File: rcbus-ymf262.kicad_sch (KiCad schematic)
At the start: 36 parts, among them CON1 SJ1-3523N, P1 RC2014 BUS, U1 74HCT688, U2 YMF262, U5 YAC512, U6 TL074, X1 14.318MHz

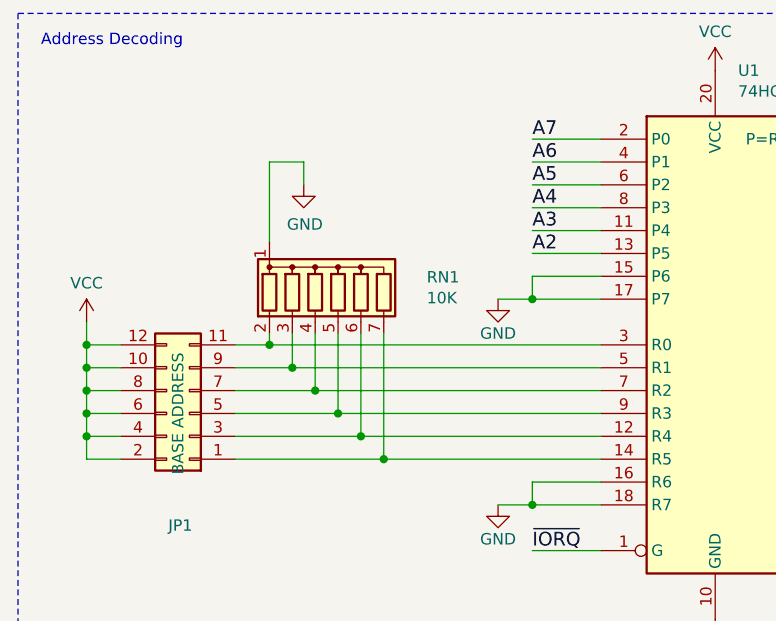
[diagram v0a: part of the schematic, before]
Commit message: some more routing, use individual resistors, change name to rcbus
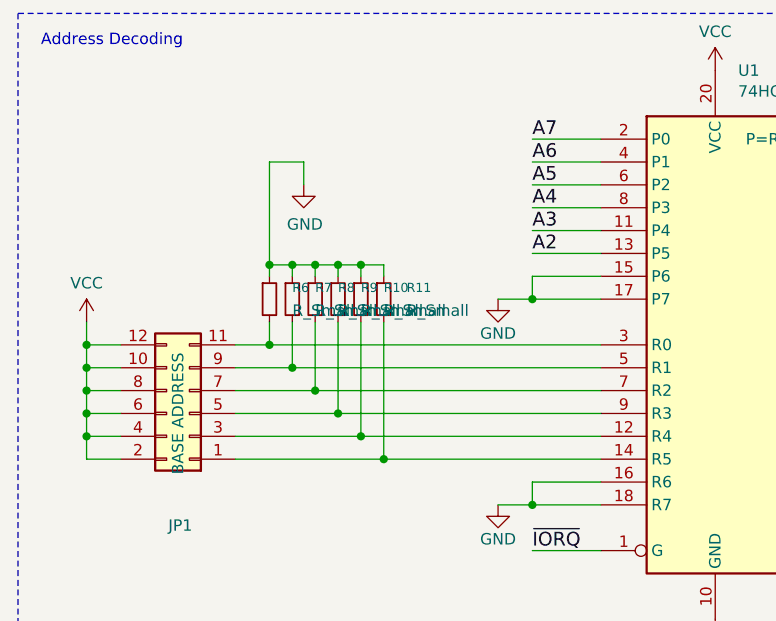
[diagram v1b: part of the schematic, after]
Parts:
- removed RN1: 10K, Resistor_SMD:R_Array_Convex_8x0602, symbol Device:R_Network06
- added R10, R11, R6, R7, R8, R9: R_Small, Resistor_SMD:R_0603_1608Metric_Pad0.98x0.95mm_HandSolder, symbol Device:R_Small
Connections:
- net GND: now also R10.1, R11.1, R6.1, R7.1, R8.1, R9.1
- net at JP1.1 (Pin_1), U1.14 (R5): now also R11.2
- net at JP1.11 (Pin_11), U1.3 (R0): now also R6.2
- net at JP1.3 (Pin_3), U1.12 (R4): now also R10.2
- net at JP1.5 (Pin_5), U1.9 (R3): now also R9.2
- net at JP1.7 (Pin_7), U1.7 (R2): now also R8.2
- net at JP1.9 (Pin_9), U1.5 (R1): now also R7.2
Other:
- title: RC2014 YM3812 sound card -> RCBUS YMF262 sound card

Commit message: more routing
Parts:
- R10, R11, R6, R7, R8, R9: value R_Small -> 10K
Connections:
- net +5V is gone; now on net VCC: C1.1, L1.2
- net GND: now also R10.2, R11.2, R6.2, R7.2, R8.2, R9.2; no longer R10.1, R11.1, R6.1, R7.1, R8.1, R9.1
- net at JP1.1 (Pin_1), U1.14 (R5): now also R11.1; no longer R11.2
- net at JP1.11 (Pin_11), U1.3 (R0): now also R6.1; no longer R6.2
- net at JP1.3 (Pin_3), U1.12 (R4): now also R10.1; no longer R10.2
- net at JP1.5 (Pin_5), U1.9 (R3): now also R9.1; no longer R9.2
- net at JP1.7 (Pin_7), U1.7 (R2): now also R8.1; no longer R8.2
- net at JP1.9 (Pin_9), U1.5 (R1): now also R7.1; no longer R7.2
- net AUDIO_CH2: now reaches C10.1, U5.11 (CH2), U6.10 (+)
- net AUDIO_CH1: now reaches C11.1, U5.10 (CH1), U6.12 (+)
- no-connect marks 21 -> 22
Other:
- moved on the sheet: C17, R10, R11, R6, R7, R8, R9

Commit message: pcb updates, remove old github actions
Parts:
- removed C15: 100nf, Capacitor_SMD:C_0603_1608Metric_Pad1.08x0.95mm_HandSolder, symbol Device:C_Small
- renumbered C2 to C1, C11 to C10, C5 to C11, C7 to C12, C16 to C13, C17 to C14, C12 to C15, C14 to C16, C18 to C17, C19 to C18, C1 to C2, C8 to C3, C9 to C4, C13 to C5, C3 to C6, C4 to C7, C6 to C8, C10 to C9, R6 to R1, R4 to R10, R5 to R11, R7 to R2, R8 to R3, R9 to R4, R10 to R5, R11 to R6, R1 to R7, R2 to R8, R3 to R9, U5 to U3, U6 to U4

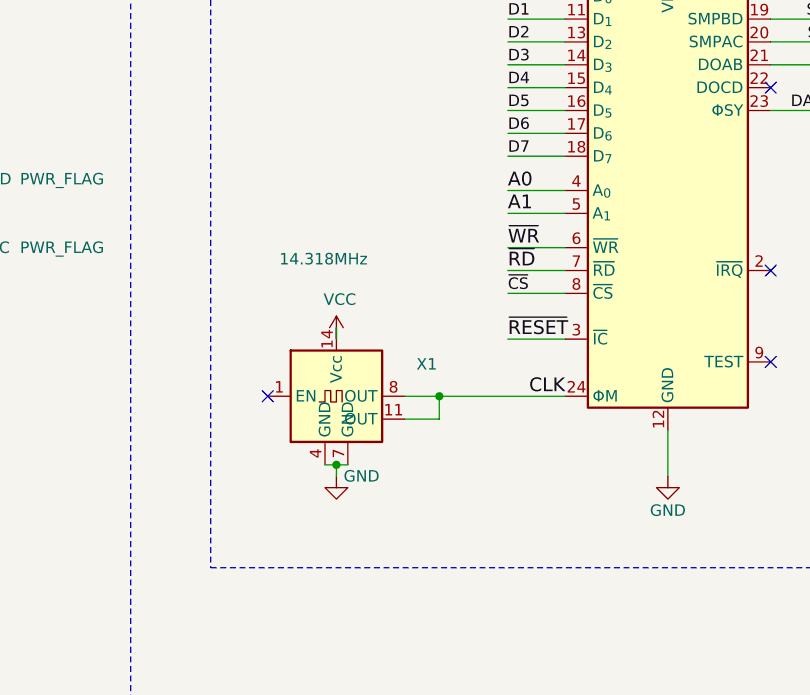
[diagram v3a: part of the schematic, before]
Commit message: use smd oscillator
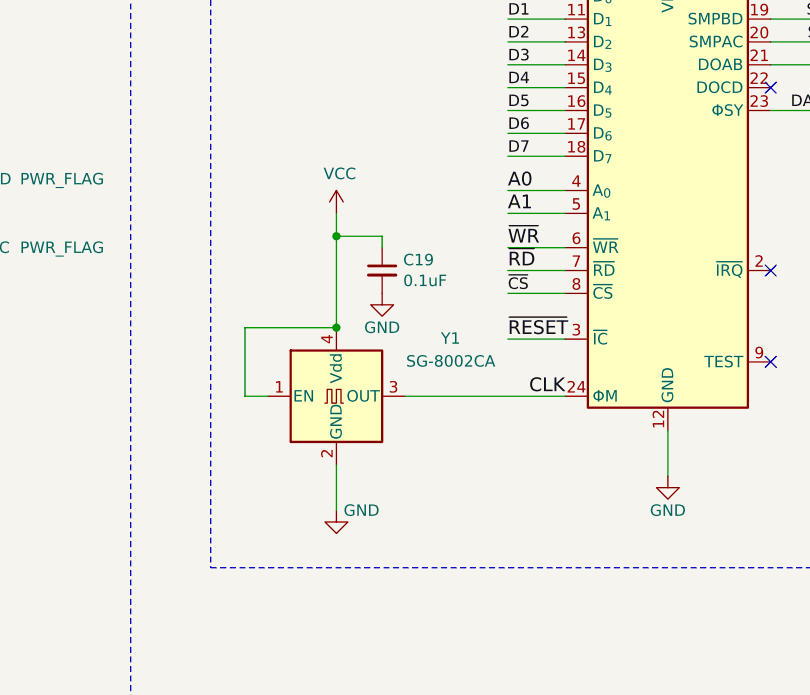
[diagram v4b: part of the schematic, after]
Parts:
- removed X1: 14.318MHz, electrified:Oscillator_DIP-8-14, symbol electrified:CXO_DIP-8-14
- added C19: 0.1uF, Capacitor_SMD:C_0603_1608Metric_Pad1.08x0.95mm_HandSolder, symbol Device:C_Small
- added Y1: SG-8002CA, Oscillator:Oscillator_SMD_Abracon_ASV-4Pin_7.0x5.1mm, symbol Oscillator:ASV-xxxMHz
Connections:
- net CLK: now also Y1.3 (OUT)
- net GND: now also C19.2, Y1.2 (GND)
- net VCC: now also C19.1, Y1.1 (EN), Y1.4 (Vdd)
- no-connect marks 22 -> 21

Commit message: set version no
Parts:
- C8: symbol Device:C_Small -> Device:C_Polarized_Small
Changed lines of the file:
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@@
 	)
 	(symbol
-		(lib_id "Device:C_Small")
+		(lib_id "Device:C_Polarized_Small")
 		(at 262.89 80.01 0)
 		(unit 1)
@@
 			)
 		)
-		(property "Description" "Unpolarized capacitor, small symbol"
+		(property "Description" "Polarized capacitor, small symbol"
 			(at 262.89 80.01 0)
 			(effects

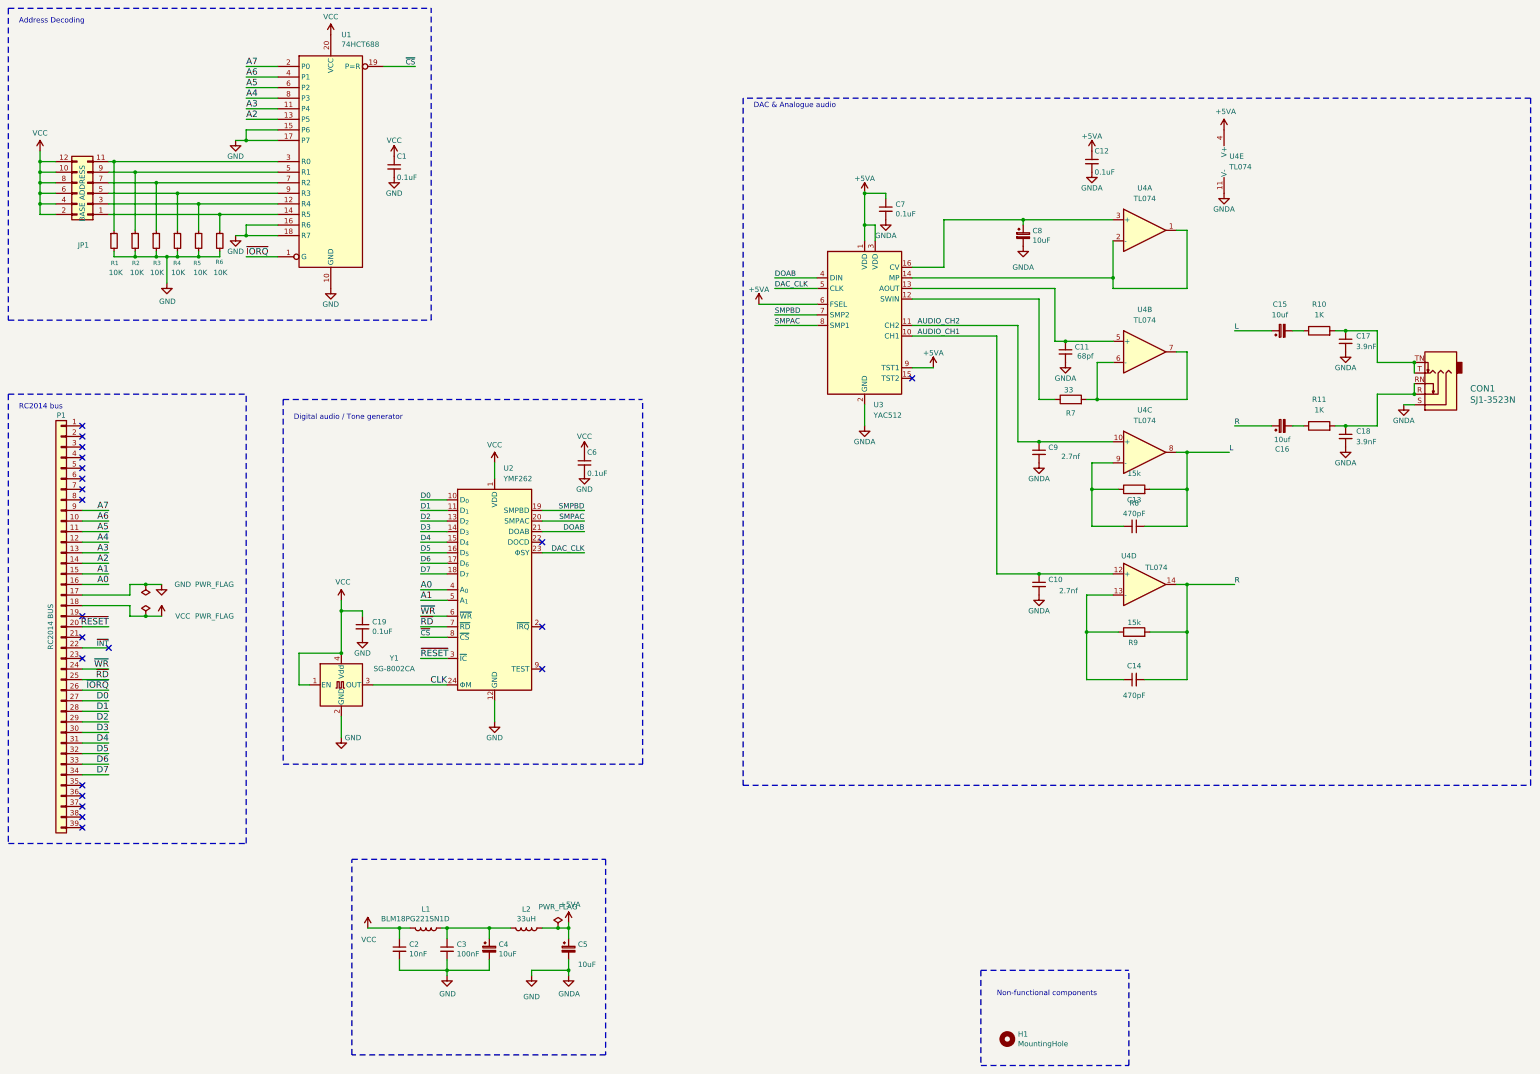
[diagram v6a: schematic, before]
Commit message: remove gnda, another attempt at versioning
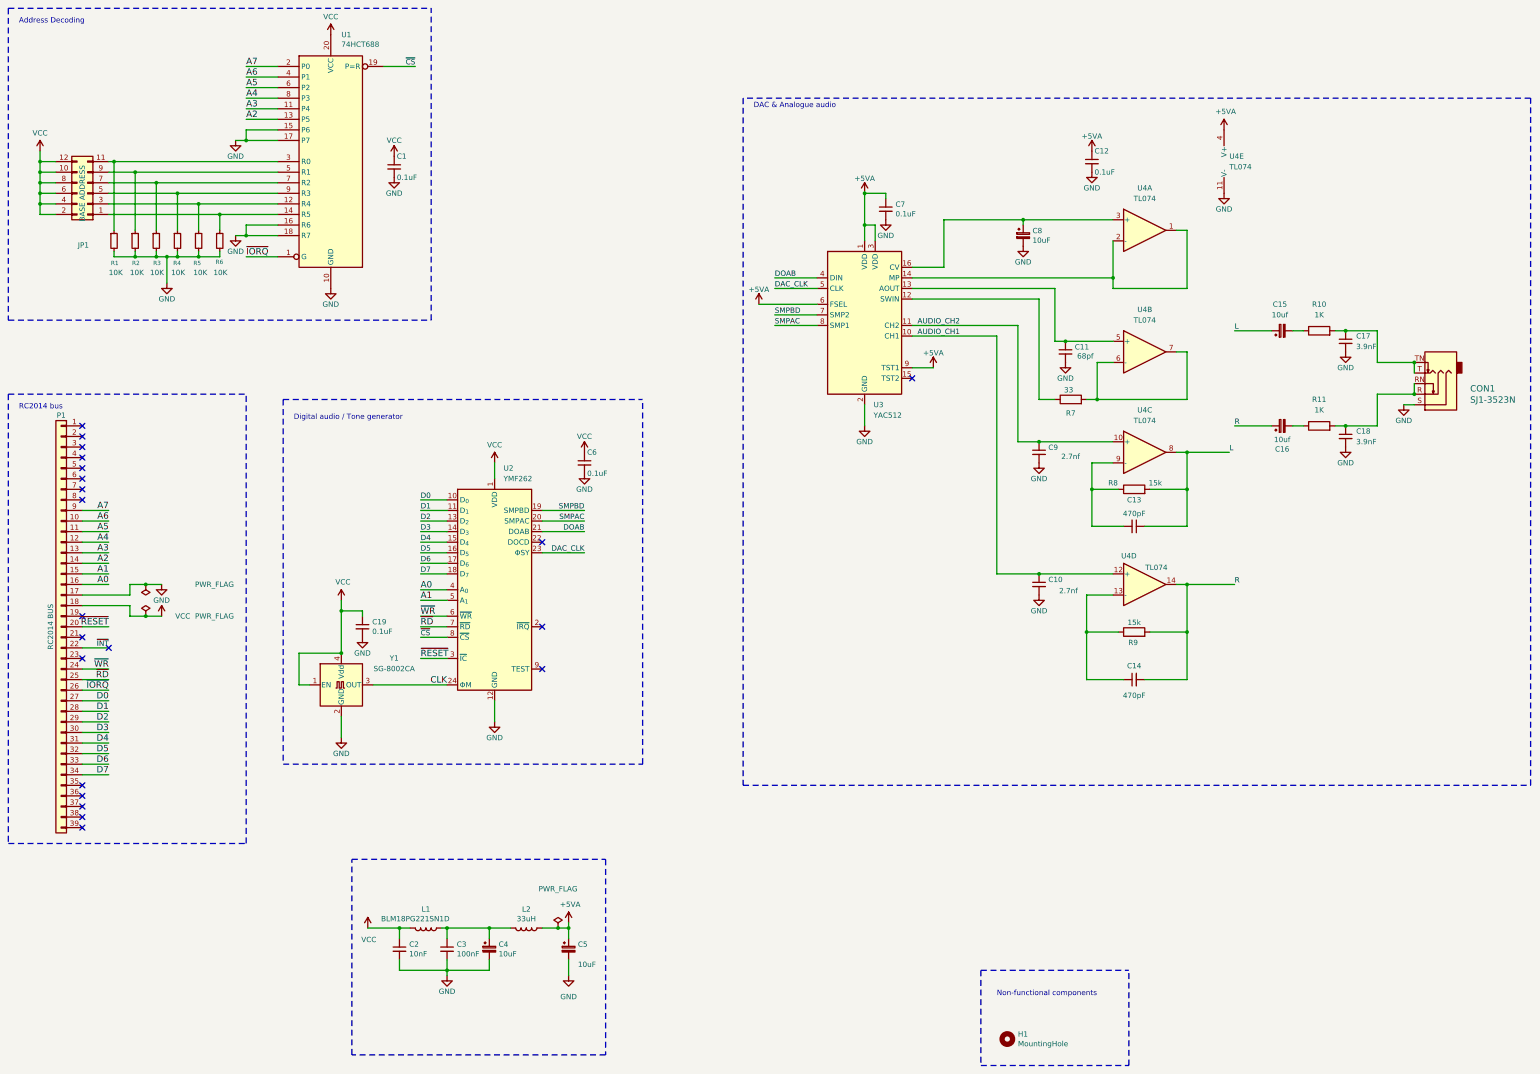
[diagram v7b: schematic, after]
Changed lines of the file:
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@@
 	)
 	(junction
-		(at 153.67 256.54)
-		(diameter 0)
-		(color 0 0 0 0)
-	)
-	(junction
 		(at 340.36 125.73)
 		(diameter 0)
@@
 	(wire
 		(pts
-			(xy 144.78 256.54) (xy 153.67 256.54)
-		)
-		(stroke
-			(width 0)
-			(type default)
-		)
-	)
-	(wire
-		(pts
 			(xy 43.18 173.99) (xy 36.83 173.99)
 		)
@@
 	(wire
 		(pts
-			(xy 144.78 257.81) (xy 144.78 256.54)
+			(xy 153.67 254) (xy 153.67 257.81)
 		)
 		(stroke
@@
 		)
 	)
-	(wire
-		(pts
-			(xy 153.67 256.54) (xy 153.67 257.81)
-		)
-		(stroke
-			(width 0)
-			(type default)
-		)
-	)
 	(polyline
 		(pts
@@
 		)
 	)
-	(wire
-		(pts
-			(xy 153.67 254) (xy 153.67 256.54)
-		)
-		(stroke
-			(width 0)
-			(type default)
-		)
-	)
 	(label "SMPAC"
 		(at 157.48 148.59 180)
@@
 		)
 		(property "Value" "GND"
-			(at 60.96 163.83 0)
+			(at 55.88 167.64 0)
 			(effects
 				(font
@@
 	)
 	(symbol
-		(lib_id "power:GNDA")
-		(at 153.67 257.81 0)
-		(unit 1)
-		(exclude_from_sim no)
-		(in_bom yes)
-		(on_board yes)
-		(dnp no)
-		(property "Reference" "#PWR019"
-			(at 153.67 264.16 0)
-			(effects
-				(font
-					(size 1.27 1.27)
-				)
-				(hide yes)
-			)
-		)
-		(property "Value" "GNDA"
-			(at 153.797 262.2042 0)
-			(effects
-				(font
-					(size 1.27 1.27)
-				)
-			)
-		)
-		(property "Footprint" ""
-			(at 153.67 257.81 0)
-			(effects
-				(font
-					(size 1.27 1.27)
-				)
-				(hide yes)
-			)
-		)
-		(property "Datasheet" ""
-			(at 153.67 257.81 0)
-			(effects
-				(font
-					(size 1.27 1.27)
-				)
-				(hide yes)
-			)
-		)
-		(property "Description" "Power symbol creates a global label with name \"GNDA\" , analog ground"
-			(at 153.67 257.81 0)
-			(effects
-				(font
-					(size 1.27 1.27)
-				)
-				(hide yes)
-			)
-		)
-		(pin "1"
-		)
-		(instances
-			(project "rc2014-ymf262"
-				(path "/9a2d648d-863a-4b7b-80f9-d537185c212b"
-					(reference "#PWR019")
-					(unit 1)
-				)
-			)
-		)
-	)
-	(symbol
 		(lib_id "power:+5VA")
 		(at 153.67 245.11 0)
@@
 		)
 		(property "Value" "GND"
-			(at 101.854 200.66 0)
+			(at 99.06 204.47 0)
 			(effects
 				(font
@@
 		)
 		(property "Value" "GND"
-			(at 57.277 95.8342 0)
+			(at 57.15 95.25 0)
 			(effects
 				(font
@@
 	)
 	(symbol
-		(lib_id "power:GNDA")
+		(lib_id "power:GND")
 		(at 224.79 125.73 0)
 		(unit 1)
@@
 			)
 		)
-		(property "Value" "GNDA"
+		(property "Value" "GND"
 			(at 224.79 129.54 0)
 			(effects
@@
 			)
 		)
-		(property "Description" "Power symbol creates a global label with name \"GNDA\" , analog ground"
+		(property "Description" "Power symbol creates a global label with name \"GND\" , ground"
 			(at 224.79 125.73 0)
 			(effects
@@
 	)
 	(symbol
-		(lib_id "power:GNDA")
+		(lib_id "power:GND")
 		(at 279.4 64.77 0)
 		(unit 1)
@@
 			)
 		)
-		(property "Value" "GNDA"
+		(property "Value" "GND"
 			(at 279.4 68.58 0)
 			(effects
@@
 			)
 		)
-		(property "Description" "Power symbol creates a global label with name \"GNDA\" , analog ground"
+		(property "Description" "Power symbol creates a global label with name \"GND\" , ground"
 			(at 279.4 64.77 0)
 			(effects
@@
 	)
 	(symbol
-		(lib_id "power:GNDA")
+		(lib_id "power:GND")
 		(at 311.15 69.85 0)
 		(unit 1)
@@
 			)
 		)
-		(property "Value" "GNDA"
+		(property "Value" "GND"
 			(at 311.15 73.66 0)
 			(effects
@@
 			)
 		)
-		(property "Description" "Power symbol creates a global label with name \"GNDA\" , analog ground"
+		(property "Description" "Power symbol creates a global label with name \"GND\" , ground"
 			(at 311.15 69.85 0)
 			(effects
@@
 	)
 	(symbol
-		(lib_id "power:GNDA")
+		(lib_id "power:GND")
 		(at 340.36 130.81 0)
 		(unit 1)
@@
 			)
 		)
-		(property "Value" "GNDA"
+		(property "Value" "GND"
 			(at 340.36 134.62 0)
 			(effects
@@
 			)
 		)
-		(property "Description" "Power symbol creates a global label with name \"GNDA\" , analog ground"
+		(property "Description" "Power symbol creates a global label with name \"GND\" , ground"
 			(at 340.36 130.81 0)
 			(effects
@@
 		(dnp no)
 		(property "Reference" "R8"
-			(at 289.56 144.272 90)
+			(at 284.48 139.446 90)
 			(effects
 				(font
@@
 		)
 		(property "Value" "15k"
-			(at 289.56 137.16 90)
+			(at 294.64 139.446 90)
 			(effects
 				(font
@@
 	)
 	(symbol
-		(lib_id "power:GNDA")
+		(lib_id "power:GND")
 		(at 340.36 107.95 0)
 		(unit 1)
@@
 			)
 		)
-		(property "Value" "GNDA"
+		(property "Value" "GND"
 			(at 340.36 111.76 0)
 			(effects
@@
 			)
 		)
-		(property "Description" "Power symbol creates a global label with name \"GNDA\" , analog ground"
+		(property "Description" "Power symbol creates a global label with name \"GND\" , ground"
 			(at 340.36 107.95 0)
 			(effects
@@
 	)
 	(symbol
-		(lib_id "power:GNDA")
+		(lib_id "power:GND")
 		(at 229.87 76.2 0)
 		(unit 1)
@@
 			)
 		)
-		(property "Value" "GNDA"
+		(property "Value" "GND"
 			(at 229.87 80.01 0)
 			(effects
@@
 			)
 		)
-		(property "Description" "Power symbol creates a global label with name \"GNDA\" , analog ground"
+		(property "Description" "Power symbol creates a global label with name \"GND\" , ground"
 			(at 229.87 76.2 0)
 			(effects
@@
 		)
 		(property "Value" "GND"
-			(at 124.587 262.2042 0)
+			(at 124.46 261.62 0)
 			(effects
 				(font
@@
 		(on_board yes)
 		(dnp no)
-		(fields_autoplaced yes)
 		(property "Reference" "#FLG03"
 			(at 151.13 244.475 0)
@@
 		)
 		(property "Value" "PWR_FLAG"
-			(at 151.13 241.3 0)
+			(at 151.13 236.982 0)
 			(effects
 				(font
@@
 	)
 	(symbol
-		(lib_id "power:GNDA")
+		(lib_id "power:GND")
 		(at 104.14 176.53 0)
 		(unit 1)
@@
 			)
 		)
-		(property "Description" "Power symbol creates a global label with name \"GNDA\" , analog ground"
+		(property "Description" "Power symbol creates a global label with name \"GND\" , ground"
 			(at 104.14 176.53 0)
 			(effects
@@
 	(symbol
 		(lib_id "power:GND")
-		(at 144.78 257.81 0)
+		(at 153.67 257.81 0)
 		(unit 1)
 		(exclude_from_sim no)
@@
 		(fields_autoplaced yes)
 		(property "Reference" "#PWR017"
-			(at 144.78 264.16 0)
+			(at 153.67 264.16 0)
 			(effects
 				(font
@@
 		)
 		(property "Value" "GND"
-			(at 144.78 262.89 0)
+			(at 153.67 262.89 0)
 			(effects
 				(font
@@
 		)
 		(property "Footprint" ""
-			(at 144.78 257.81 0)
+			(at 153.67 257.81 0)
 			(effects
 				(font
@@
 		)
 		(property "Datasheet" ""
-			(at 144.78 257.81 0)
+			(at 153.67 257.81 0)
 			(effects
 				(font
@@
 		)
 		(property "Description" "Power symbol creates a global label with name \"GND\" , ground"
-			(at 144.78 257.81 0)
+			(at 153.67 257.81 0)
 			(effects
 				(font
@@
 	)
 	(symbol
-		(lib_id "power:GNDA")
+		(lib_id "power:GND")
 		(at 262.89 82.55 0)
 		(unit 1)
@@
 			)
 		)
-		(property "Value" "GNDA"
-			(at 262.89 87.63 0)
+		(property "Value" "GND"
+			(at 262.89 86.36 0)
 			(effects
 				(font
@@
 			)
 		)
-		(property "Description" "Power symbol creates a global label with name \"GNDA\" , analog ground"
+		(property "Description" "Power symbol creates a global label with name \"GND\" , ground"
 			(at 262.89 82.55 0)
 			(effects
@@
 	)
 	(symbol
-		(lib_id "power:GNDA")
+		(lib_id "power:GND")
 		(at 266.7 166.37 0)
 		(unit 1)
@@
 			)
 		)
-		(property "Value" "GNDA"
+		(property "Value" "GND"
 			(at 266.7 170.18 0)
 			(effects
@@
 			)
 		)
-		(property "Description" "Power symbol creates a global label with name \"GNDA\" , analog ground"
+		(property "Description" "Power symbol creates a global label with name \"GND\" , ground"
 			(at 266.7 166.37 0)
 			(effects
@@
 	)
 	(symbol
-		(lib_id "power:GNDA")
+		(lib_id "power:GND")
 		(at 273.05 110.49 0)
 		(unit 1)
@@
 			)
 		)
-		(property "Value" "GNDA"
+		(property "Value" "GND"
 			(at 273.05 114.3 0)
 			(effects
@@
 			)
 		)
-		(property "Description" "Power symbol creates a global label with name \"GNDA\" , analog ground"
+		(property "Description" "Power symbol creates a global label with name \"GND\" , ground"
 			(at 273.05 110.49 0)
 			(effects
@@
 	)
 	(symbol
-		(lib_id "power:GNDA")
+		(lib_id "power:GND")
 		(at 354.33 120.65 0)
 		(unit 1)
@@
 			)
 		)
-		(property "Value" "GNDA"
+		(property "Value" "GND"
 			(at 354.33 124.46 0)
 			(effects
@@
 			)
 		)
-		(property "Description" "Power symbol creates a global label with name \"GNDA\" , analog ground"
+		(property "Description" "Power symbol creates a global label with name \"GND\" , ground"
 			(at 354.33 120.65 0)
 			(effects
@@
 	)
 	(symbol
-		(lib_id "power:GNDA")
+		(lib_id "power:GND")
 		(at 266.7 134.62 0)
 		(unit 1)
@@
 			)
 		)
-		(property "Value" "GNDA"
+		(property "Value" "GND"
 			(at 266.7 138.43 0)
 			(effects
@@
 			)
 		)
-		(property "Description" "Power symbol creates a global label with name \"GNDA\" , analog ground"
+		(property "Description" "Power symbol creates a global label with name \"GND\" , ground"
 			(at 266.7 134.62 0)
 			(effects
